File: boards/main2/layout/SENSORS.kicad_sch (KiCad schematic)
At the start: 54 parts, among them IC2 LSM6DSVTR, Q2 AO3400A, Q3 AO3400A, Q4 AO3400A, Q5 AO3400A, Q9 AO3400A, U10 INA241A2IDGKR, U11 INA241A2IDGKR, U12 TLV9001IDBVR

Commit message: 🐛 Keep main2's root labels on the page
SENSORS took three Spi ports, one per device, so the shared SCK, MISO and MOSI came in three times: 32 sheet pins. pcb 0.4.81 places the root's sheet symbols one by one in the order of their names, each as near the page centre as the earlier ones leave room and by its box alone, and a 32-pin SENSORS fitted only against the page's left edge, where the labels at its pins ran up to 11 mm past the page.

SENSORS now takes the bus once (SPI_SCK, SPI_MISO, SPI_MOSI) and each device's chip select (IMU_SPI_CSn, Encoder_Right_CSn, Encoder_Left_CSn), and builds the three Spi interfaces inside. With 26 pins it sits right of ESP, and every label is on its page, so the strict xfail in tests/test_schematic.py goes. The ports take their nets' names, which leaves 8 multiple_net_names warnings instead of 14. The netlist is unchanged: the same 174 nets with the same names and pins.
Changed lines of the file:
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@@
 		)
 	)
-	(hierarchical_label "ENCODER_LEFT_SPI.CLK"
+	(hierarchical_label "Encoder_Left_ABI_A"
+		(shape bidirectional)
+		(at 179.07 165.1 0)
+		(effects
+			(font
+				(size 1.27 1.27)
+			)
+			(justify left)
+		)
+	)
+	(hierarchical_label "SPI_SCK"
 		(shape bidirectional)
 		(at 96.52 162.56 180)
@@
 		)
 	)
-	(hierarchical_label "Encoder_Left_ABI_A"
-		(shape bidirectional)
-		(at 179.07 165.1 0)
-		(effects
-			(font
-				(size 1.27 1.27)
-			)
-			(justify left)
-		)
-	)
-	(hierarchical_label "IMU_SPI.MOSI"
+	(hierarchical_label "Wall_Sensor_3"
+		(shape bidirectional)
+		(at 106.68 500.38 90)
+		(effects
+			(font
+				(size 1.27 1.27)
+			)
+			(justify left)
+		)
+	)
+	(hierarchical_label "IMU_INT2"
+		(shape bidirectional)
+		(at 755.65 91.44 0)
+		(effects
+			(font
+				(size 1.27 1.27)
+			)
+			(justify left)
+		)
+	)
+	(hierarchical_label "Wall_Sensor_0"
+		(shape bidirectional)
+		(at 142.24 466.09 90)
+		(effects
+			(font
+				(size 1.27 1.27)
+			)
+			(justify left)
+		)
+	)
+	(hierarchical_label "SPI_MISO"
+		(shape bidirectional)
+		(at 96.52 165.1 180)
+		(effects
+			(font
+				(size 1.27 1.27)
+			)
+			(justify right)
+		)
+	)
+	(hierarchical_label "SPI_MOSI"
 		(shape bidirectional)
 		(at 96.52 167.64 180)
@@
 		)
 	)
-	(hierarchical_label "IMU_SPI.CS"
+	(hierarchical_label "Encoder_Right_ABI_A"
+		(shape bidirectional)
+		(at 116.84 165.1 0)
+		(effects
+			(font
+				(size 1.27 1.27)
+			)
+			(justify left)
+		)
+	)
+	(hierarchical_label "IMU_SPI_CSn"
 		(shape bidirectional)
 		(at 735.33 96.52 180)
@@
 		)
 	)
-	(hierarchical_label "ENCODER_LEFT_SPI.CLK"
-		(shape bidirectional)
-		(at 96.52 162.56 180)
-		(effects
-			(font
-				(size 1.27 1.27)
-			)
-			(justify right)
-		)
-	)
-	(hierarchical_label "Wall_Sensor_3"
-		(shape bidirectional)
-		(at 106.68 500.38 90)
-		(effects
-			(font
-				(size 1.27 1.27)
-			)
-			(justify left)
-		)
-	)
-	(hierarchical_label "IMU_INT2"
-		(shape bidirectional)
-		(at 755.65 91.44 0)
-		(effects
-			(font
-				(size 1.27 1.27)
-			)
-			(justify left)
-		)
-	)
-	(hierarchical_label "Wall_Sensor_0"
-		(shape bidirectional)
-		(at 142.24 466.09 90)
-		(effects
-			(font
-				(size 1.27 1.27)
-			)
-			(justify left)
-		)
-	)
-	(hierarchical_label "IMU_SPI.MISO"
-		(shape bidirectional)
-		(at 96.52 165.1 180)
-		(effects
-			(font
-				(size 1.27 1.27)
-			)
-			(justify right)
-		)
-	)
-	(hierarchical_label "ENCODER_RIGHT_SPI.CLK"
-		(shape bidirectional)
-		(at 96.52 162.56 180)
-		(effects
-			(font
-				(size 1.27 1.27)
-			)
-			(justify right)
-		)
-	)
-	(hierarchical_label "ENCODER_LEFT_SPI.CLK"
-		(shape bidirectional)
-		(at 96.52 162.56 180)
-		(effects
-			(font
-				(size 1.27 1.27)
-			)
-			(justify right)
-		)
-	)
-	(hierarchical_label "Encoder_Right_ABI_A"
-		(shape bidirectional)
-		(at 116.84 165.1 0)
-		(effects
-			(font
-				(size 1.27 1.27)
-			)
-			(justify left)
-		)
-	)
-	(hierarchical_label "ENCODER_LEFT_SPI.MOSI"
-		(shape bidirectional)
-		(at 96.52 167.64 180)
-		(effects
-			(font
-				(size 1.27 1.27)
-			)
-			(justify right)
-		)
-	)
-	(hierarchical_label "ENCODER_LEFT_SPI.MOSI"
-		(shape bidirectional)
-		(at 96.52 167.64 180)
-		(effects
-			(font
-				(size 1.27 1.27)
-			)
-			(justify right)
-		)
-	)
 	(hierarchical_label "Wall_Sensor_PWM_2"
 		(shape bidirectional)
@@
 		)
 	)
-	(hierarchical_label "ENCODER_RIGHT_SPI.CS"
+	(hierarchical_label "Encoder_Left_CSn"
+		(shape bidirectional)
+		(at 158.75 160.02 180)
+		(effects
+			(font
+				(size 1.27 1.27)
+			)
+			(justify right)
+		)
+	)
+	(hierarchical_label "Wall_Sensor_1"
+		(shape bidirectional)
+		(at 158.75 466.09 90)
+		(effects
+			(font
+				(size 1.27 1.27)
+			)
+			(justify left)
+		)
+	)
+	(hierarchical_label "Encoder_Right_CSn"
 		(shape bidirectional)
 		(at 96.52 160.02 180)
@@
 		)
 	)
-	(hierarchical_label "Wall_Sensor_1"
-		(shape bidirectional)
-		(at 158.75 466.09 90)
-		(effects
-			(font
-				(size 1.27 1.27)
-			)
-			(justify left)
-		)
-	)
-	(hierarchical_label "IMU_SPI.CLK"
-		(shape bidirectional)
-		(at 96.52 162.56 180)
-		(effects
-			(font
-				(size 1.27 1.27)
-			)
-			(justify right)
-		)
-	)
 	(hierarchical_label "MOTOR_R_SENSE_P"
 		(shape bidirectional)
@@
 		)
 	)
-	(hierarchical_label "ENCODER_LEFT_SPI.MISO"
-		(shape bidirectional)
-		(at 96.52 165.1 180)
-		(effects
-			(font
-				(size 1.27 1.27)
-			)
-			(justify right)
-		)
-	)
-	(hierarchical_label "ENCODER_LEFT_SPI.MISO"
-		(shape bidirectional)
-		(at 96.52 165.1 180)
-		(effects
-			(font
-				(size 1.27 1.27)
-			)
-			(justify right)
-		)
-	)
-	(hierarchical_label "ENCODER_LEFT_SPI.CS"
-		(shape bidirectional)
-		(at 158.75 160.02 180)
-		(effects
-			(font
-				(size 1.27 1.27)
-			)
-			(justify right)
-		)
-	)
 	(hierarchical_label "MOTOR_R_SENSE_N"
 		(shape bidirectional)
@@
 		)
 	)
-	(hierarchical_label "ENCODER_RIGHT_SPI.MOSI"
-		(shape bidirectional)
-		(at 96.52 167.64 180)
-		(effects
-			(font
-				(size 1.27 1.27)
-			)
-			(justify right)
-		)
-	)
 	(hierarchical_label "Wall_Sensor_2"
 		(shape bidirectional)
@@
 		)
 	)
-	(hierarchical_label "ENCODER_RIGHT_SPI.MISO"
-		(shape bidirectional)
-		(at 96.52 165.1 180)
-		(effects
-			(font
-				(size 1.27 1.27)
-			)
-			(justify right)
-		)
-	)
 	(hierarchical_label "Current_Sensor_Right"
 		(shape bidirectional)
@@
 		)
 	)
-	(hierarchical_label "ENCODER_LEFT_SPI.MOSI"
-		(shape bidirectional)
-		(at 96.52 167.64 180)
-		(effects
-			(font
-				(size 1.27 1.27)
-			)
-			(justify right)
-		)
-	)
-	(hierarchical_label "ENCODER_LEFT_SPI.MISO"
-		(shape bidirectional)
-		(at 96.52 165.1 180)
-		(effects
-			(font
-				(size 1.27 1.27)
-			)
-			(justify right)
-		)
-	)

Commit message: 🎨 Place main2's SENSORS sheet, and draw the TLV9001's inputs as + and − in its triangle
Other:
- note added: "Emitter current sink: TLV9001 + AO3400A, 0.21 V / 1.2 Ohm = 175 mA"
- note added: "Encoder slot EC1: right wheel"
- note added: "Encoder slot EC2: left wheel"
- note added: "IMU: LSM6DSV on the SPI bus, mode 1 (SDx, SCx grounded)"
- note added: "Motor current, left motor: U11 INA241A2, 20 V/V, mid-supply reference"
- note added: "Motor current, right motor: U10 INA241A2, 20 V/V, mid-supply reference"
- note added: "Sheet ports"
- note added: "Wall sensor 0: W1, emitter selector Q2, receiver load R14"
- note added: "Wall sensor 1: W2, emitter selector Q3, receiver load R18"
- note added: "Wall sensor 2: W3, emitter selector Q4, receiver load R22"
- note added: "Wall sensor 3: W4, emitter selector Q5, receiver load R26"
- title: (none) -> Sensors: IMU, encoders, motor current, wall sensors
- moved on the sheet: C100, C101, C102, C103, C104, C105, C106, C24, C25, C26, C27, C28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

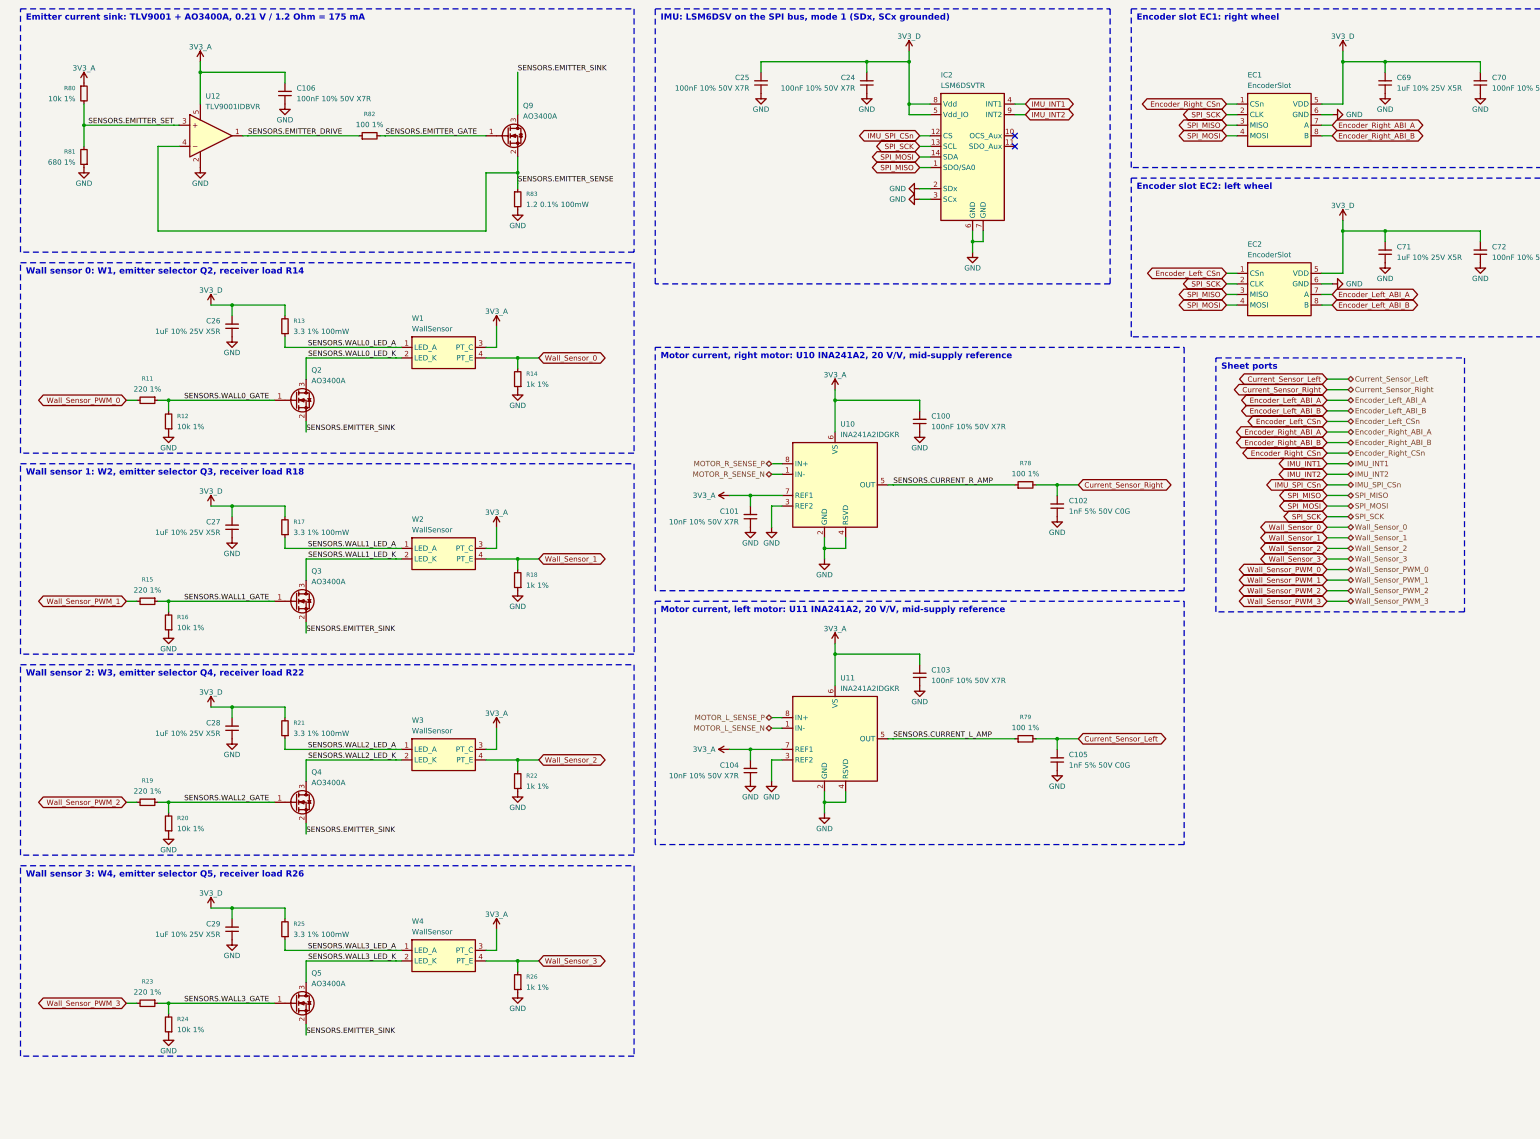
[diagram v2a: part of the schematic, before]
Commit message: ✨ Set main2's emitter current from the DAC and AC-couple its selectors
- The shared sink's set-point comes from PA5 (DAC1_OUT2, buffer off) through
  200k/20k, ratiometric to VDDA and 0 V at reset; 1k/1 nF compensates the loop
  into Q9 and 200k from 3V3_A turns the sink off at a zero set-point.
- Q2-Q5 keep the main board's AC-coupled gates (220 nF, 22k, 1N4148WS clamp):
  a pin held high turns its emitter off within 11 ms.
- Battery_Voltage moves to PC5, Switch_0 to PH0; the H7's VBUS divider goes,
  the ESP32 reports USB power over UART4.
- A test bench checks the selector coupling and the DAC set-point; the
  research model is calculations/emitter/emitter_sink.py.
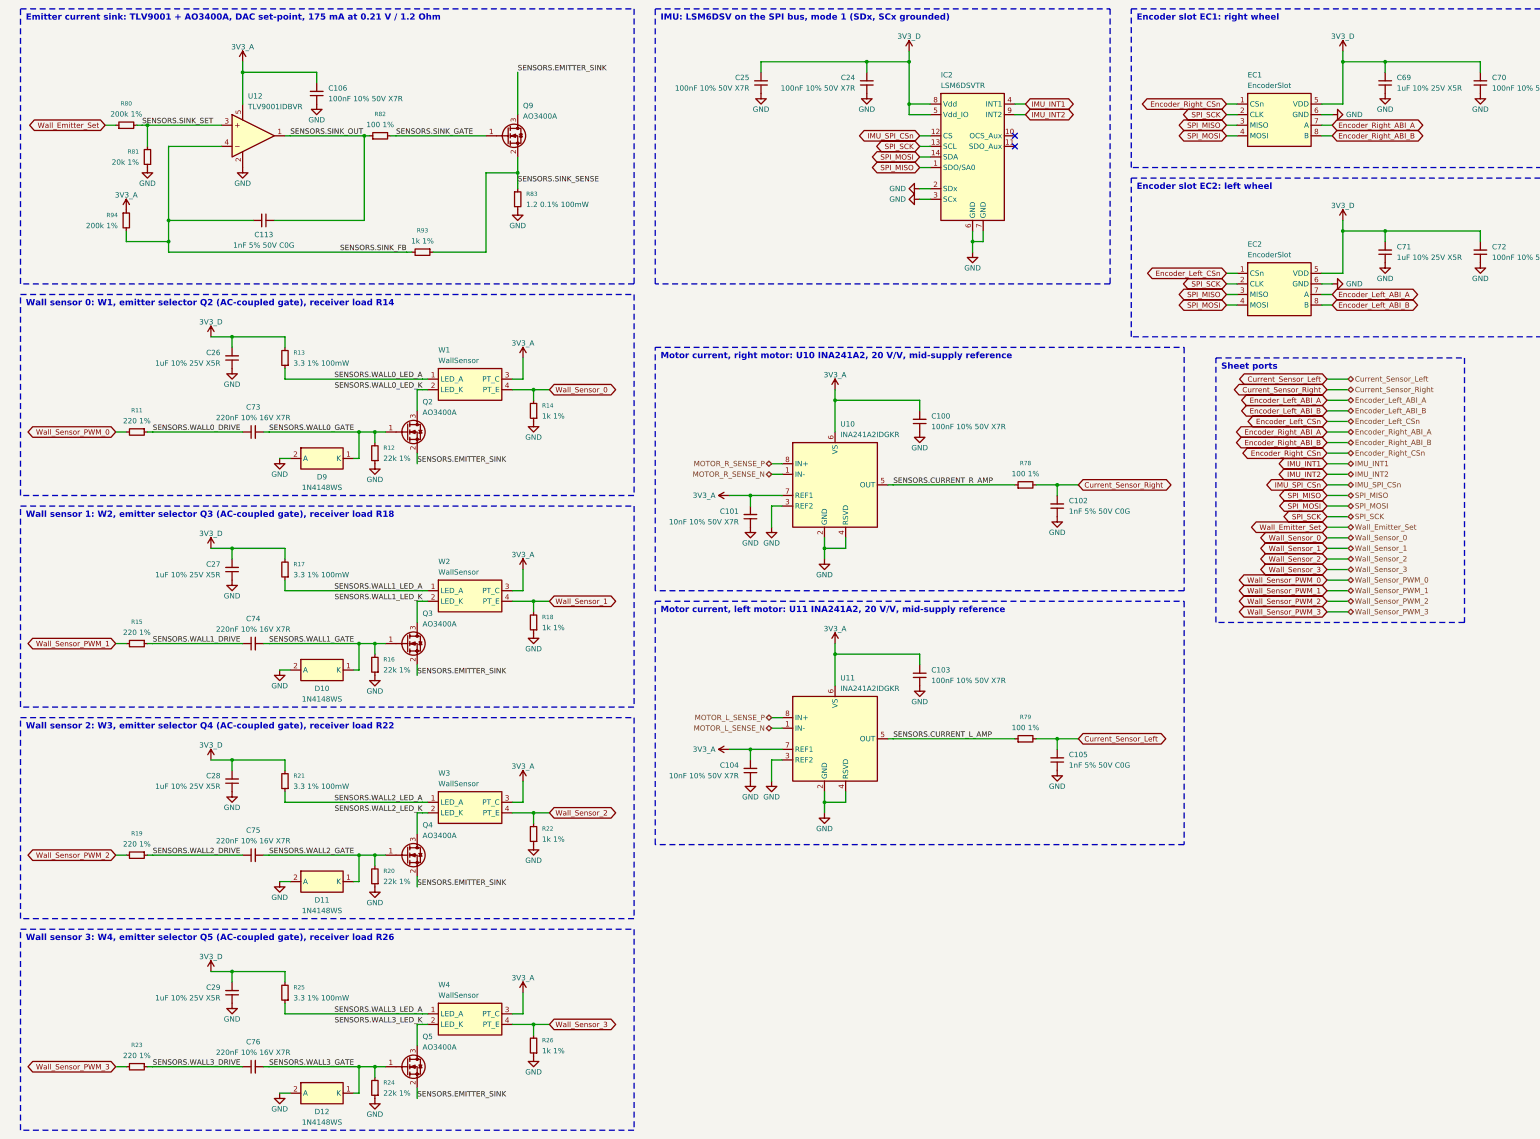
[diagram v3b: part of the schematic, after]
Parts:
- added C113: 1nF 5% 50V C0G, stdlib_kicad-footprints_Capacitor_SMD:C_0402_1005Metric, symbol C_Small
- added C73, C74, C75, C76: 220nF 10% 16V X7R, stdlib_kicad-footprints_Capacitor_SMD:C_0402_1005Metric, symbol C_Small
- added D10, D11, D12, D9: 1N4148WS, Team-Micras_MicrasPCB_components_cj_1N4148WS:D_SOD-323, symbol 1N4148WS
- added R93: 1k 1%, stdlib_kicad-footprints_Resistor_SMD:R_0402_1005Metric, symbol R_Small
- added R94: 200k 1%, stdlib_kicad-footprints_Resistor_SMD:R_0402_1005Metric, symbol R_Small
- R12, R16, R20, R24: value 10k 1% -> 22k 1%
- R80: value 10k 1% -> 200k 1%
- R81: value 680 1% -> 20k 1%
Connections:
- net 3V3_A: now also R94.1; no longer R80.1
- net GND: now also D10.2 (A), D11.2 (A), D12.2 (A), D9.2 (A)
- net SENSORS.WALL0_GATE: now also C73.2, D9.1 (K); no longer R11.1
- net SENSORS.WALL1_GATE: now also C74.2, D10.1 (K); no longer R15.1
- net SENSORS.WALL2_GATE: now also C75.2, D11.1 (K); no longer R19.1
- net SENSORS.WALL3_GATE: now also C76.2, D12.1 (K); no longer R23.1
- net SENSORS.EMITTER_DRIVE renamed SENSORS.SINK_OUT
- net SENSORS.SINK_OUT: now also C113.1
- net SENSORS.EMITTER_GATE renamed SENSORS.SINK_GATE
- net SENSORS.EMITTER_SENSE renamed SENSORS.SINK_SENSE
- net SENSORS.SINK_SENSE: now also R93.1; no longer U12.4 (-)
- net SENSORS.EMITTER_SET renamed SENSORS.SINK_SET
- new net SENSORS.SINK_FB: C113.2, R93.2, R94.2, U12.4 (-)
- new net SENSORS.WALL0_DRIVE: C73.1, R11.1
- new net SENSORS.WALL1_DRIVE: C74.1, R15.1
- new net SENSORS.WALL2_DRIVE: C75.1, R19.1
- new net SENSORS.WALL3_DRIVE: C76.1, R23.1
- new net Wall_Emitter_Set: R80.1
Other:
- note added: "Emitter current sink: TLV9001 + AO3400A, DAC set-point, 175 mA at 0.21 V / 1.2 Ohm"
- note added: "Wall sensor 0: W1, emitter selector Q2 (AC-coupled gate), receiver load R14"
- note added: "Wall sensor 1: W2, emitter selector Q3 (AC-coupled gate), receiver load R18"
- note added: "Wall sensor 2: W3, emitter selector Q4 (AC-coupled gate), receiver load R22"
- note added: "Wall sensor 3: W4, emitter selector Q5 (AC-coupled gate), receiver load R26"
- note removed: "Emitter current sink: TLV9001 + AO3400A, 0.21 V / 1.2 Ohm = 175 mA"
- note removed: "Wall sensor 0: W1, emitter selector Q2, receiver load R14"
- note removed: "Wall sensor 1: W2, emitter selector Q3, receiver load R18"
- note removed: "Wall sensor 2: W3, emitter selector Q4, receiver load R22"
- note removed: "Wall sensor 3: W4, emitter selector Q5, receiver load R26"
- moved on the sheet: C106, C26, C27, C28, C29, Q2, Q3, Q4, Q5, R11, R12, R13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

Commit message: 🐛 Fix main2's review findings and settle its open doubts
Schematic and parts:
- Battery input: F1 is a 12 A Littelfuse 501 (0501012.WR1). C58 now sits
  gate-source with C114 gate-drain, so Q6 stays off at plug-in. D16 clamps
  Q8's VGS. R44/R45 are 10k/2k, so VBAT can't float up on USB alone.
- Capacitors: VBAT and VSYS use 1210/0805 50 V parts, sized with Samsung's
  DC-bias curves. C109 is fitted.
- Drivers: R66/R76 are removed (the chokes are needed). ITRIP and the fan
  limit are retuned. The INA241 R_iso is 150 Ohm.
- Rails are declared as ranges, and the abs-max checks run under the TVS
  clamp.
- STM32 pin swaps for routing: the wall selectors move to TIM3,
  Motor_Left_EN to TIM8_CH2 and LED_ARGB to TIM17. CubeMX 6.18.1 confirms
  the map.
- firmware_changes.toml registers the matching firmware changes: the ADC
  0.7 us sampling time, the TIM4-triggered DAC, the fan's 50 kHz start, a
  wheel-sign self-check, VDDA tracking, contest mode, the debug halt and
  others.

Layout:
- USB D+/D- are routed as a coupled pair. The track floor is 0.12 mm.
- Stubs and detours are trimmed. The In2 VCORE/3V3_D islands are shrunk.
- The board is notched under the ESP32 antenna.
- Ground stitching, thermal reliefs, open thermal vias with split paste,
  DRV8874 heat islands and teardrops are added.
- 11 joins remain for hand-routing (layout README, Open items).

Doubts are closed by datasheets, vendor SPICE models and new research
calculations instead of bench TODOs. Tests cover each review item.
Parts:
- removed C101, C104: 10nF 10% 50V X7R, stdlib_kicad-footprints_Capacitor_SMD:C_0402_1005Metric, symbol C_Small
- R78, R79: value 100 1% -> 150 1%
